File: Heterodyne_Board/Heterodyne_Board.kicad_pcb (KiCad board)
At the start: 2 copper layers, 47 parts, among them J1 AVR-ISP-6, J2 Speaker, J3 SWITCH, U1 ATtiny85-20P, U2 TLV9054xD, U3 AP2112K-3.3, U4 LM386, U5 W25X40CLSN

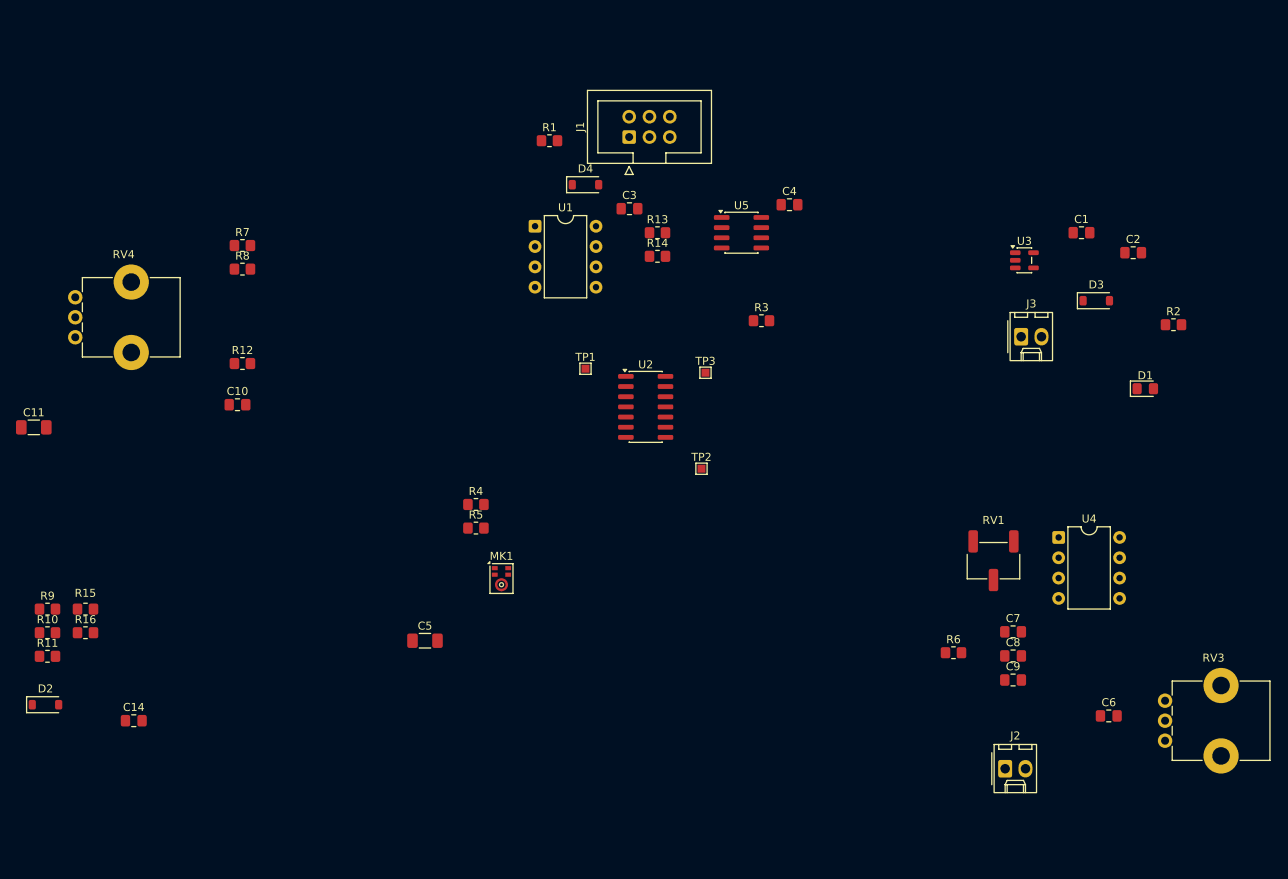
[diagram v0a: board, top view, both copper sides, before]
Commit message: continued PCB design
modules organized except for audio amp, no wiring yet
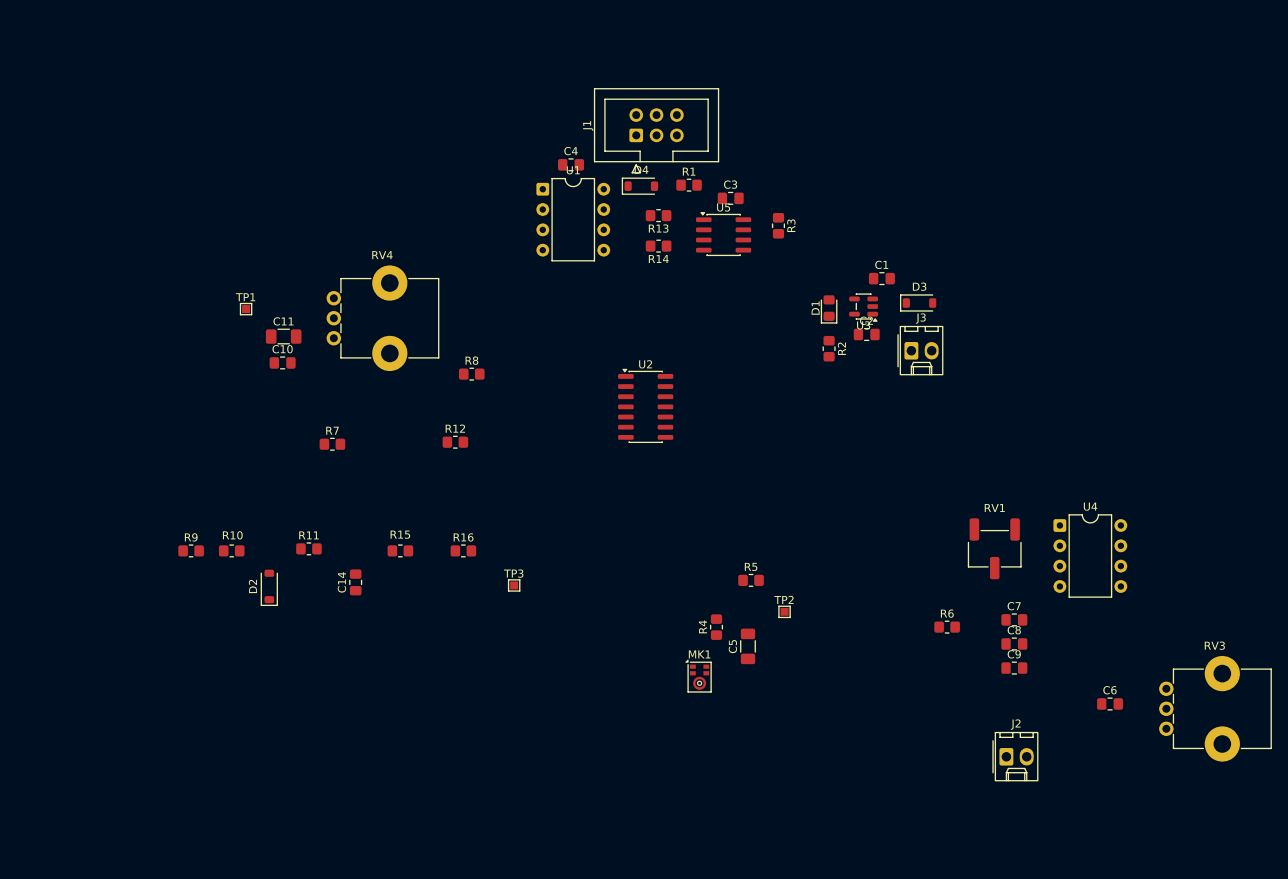
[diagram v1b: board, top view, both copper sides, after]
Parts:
- moved R16 48.3 mm to (121.8, 96.8)
- moved R2 43.2 mm to (167.5, 71.5), turned to -90 degrees
- moved TP1 43.1 mm to (94.6, 66.5)
- moved D1 40.8 mm to (167.5, 66.4), turned to 90 degrees
- moved C5 40.4 mm to (157.4, 108.7), turned to 90 degrees
- moved R15 40.0 mm to (113.9, 96.8)
- moved TP3 35.8 mm to (128.1, 101.1)
- moved R11 35.3 mm to (102.5, 96.5)
- moved R5 35.0 mm to (157.7, 100.5)
- moved C2 34.8 mm to (172.2, 69.7)
- moved R4 33.8 mm to (153.4, 106.3), turned to 90 degrees
- moved C11 33.2 mm to (99.3, 70.0)
- moved C14 32.7 mm to (108.3, 100.7), turned to 90 degrees
- moved RV4 32.3 mm to (105.6, 70.2)
- moved D2 31.6 mm to (97.5, 101.2), turned to 90 degrees
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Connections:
- RV4 pad 2: unconnected-(RV4-Pad2) -> Net-(R8-Pad2)
- RV4 pad 3: Net-(R8-Pad2) -> unconnected-(RV4-Pad3)

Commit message: finished the basic PCB layout
no wiring has been done yet though
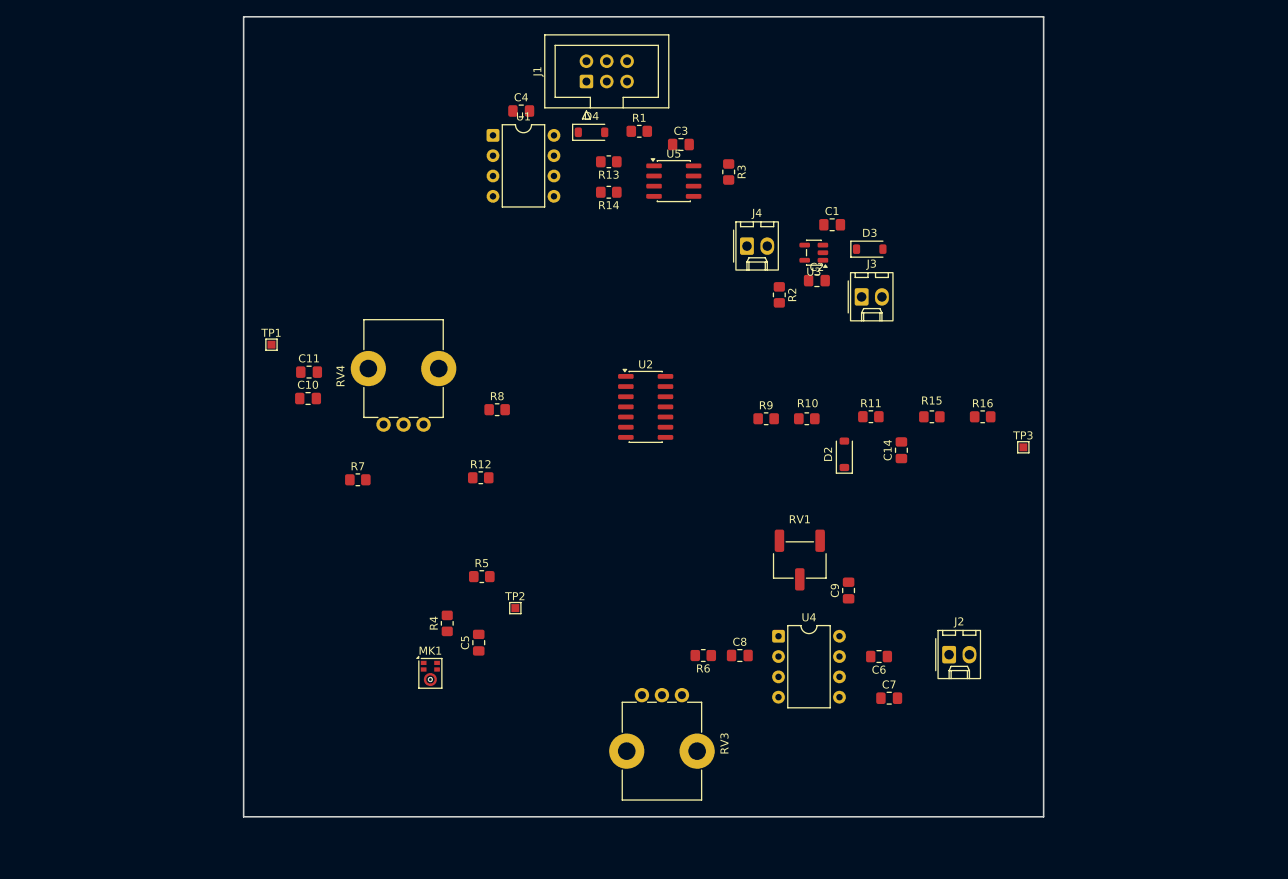
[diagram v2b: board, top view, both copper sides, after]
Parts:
- removed D1: LED, LED_SMD:LED_0805_2012Metric_Pad1.15x1.40mm_HandSolder
- added J4: LED, Connector_Molex:Molex_KK-254_AE-6410-02A_1x02_P2.54mm_Vertical, F.Cu at (157.2, 58.7)
- C11, C5: footprint Capacitor_SMD:C_1206_3216Metric_Pad1.33x1.80mm_HandSolder -> Capacitor_SMD:C_0805_2012Metric_Pad1.18x1.45mm_HandSolder
- moved R10 73.8 mm to (164.7, 80.3)
- moved D2 73.8 mm to (169.4, 84.7)
- moved R9 73.8 mm to (159.6, 80.3)
- moved R11 72.2 mm to (172.7, 80.0)
- moved C14 70.2 mm to (176.5, 84.2)
- moved R15 68.5 mm to (180.3, 80.0)
- moved R16 67.0 mm to (186.7, 80.0)
- moved TP3 65.9 mm to (191.8, 83.8)
- moved RV3 65.7 mm to (144.1, 114.8), turned to -90 degrees
- moved U4 37.8 mm to (161.2, 107.4)
- moved C8 34.3 mm to (156.3, 109.9)
- moved C5 33.7 mm to (123.7, 108.2)
- moved R5 33.7 mm to (124.1, 100.0)
- moved MK1 33.7 mm to (117.7, 112.1)
- moved R4 33.7 mm to (119.8, 105.8)
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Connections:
- R4 pad 2: Net-(U2C--) -> Net-(U2B--)
- R5 pad 1: Net-(U2C--) -> Net-(U2B--)
- U2 pad 10: +3V3 -> unconnected-(U2C-+-Pad10)
- U2 pad 5: unconnected-(U2B-+-Pad5) -> +3V3
- U2 pad 6: unconnected-(U2B---Pad6) -> Net-(U2B--)
- U2 pad 7: unconnected-(U2-Pad7) -> /Mic_out
- U2 pad 8: /Mic_out -> unconnected-(U2-Pad8)
- U2 pad 9: Net-(U2C--) -> unconnected-(U2C---Pad9)
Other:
- board outline added: 100 x 100 mm

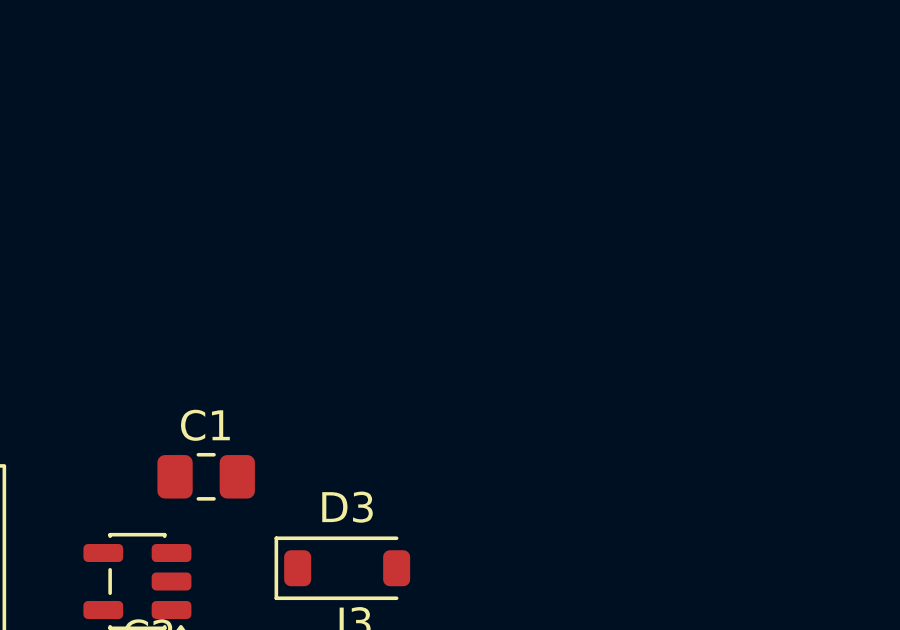
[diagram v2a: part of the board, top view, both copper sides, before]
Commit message: added two new testpoints
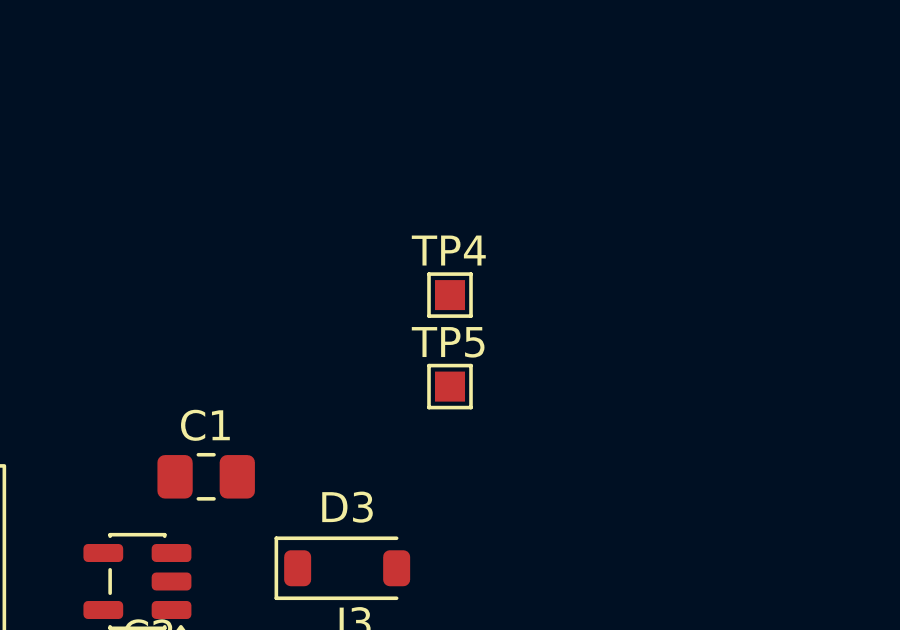
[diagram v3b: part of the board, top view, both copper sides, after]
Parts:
- added TP4: TestPoint, TestPoint:TestPoint_Pad_1.0x1.0mm, F.Cu at (176.0, 50.0)
- added TP5: TestPoint, TestPoint:TestPoint_Pad_1.0x1.0mm, F.Cu at (176.0, 53.0)

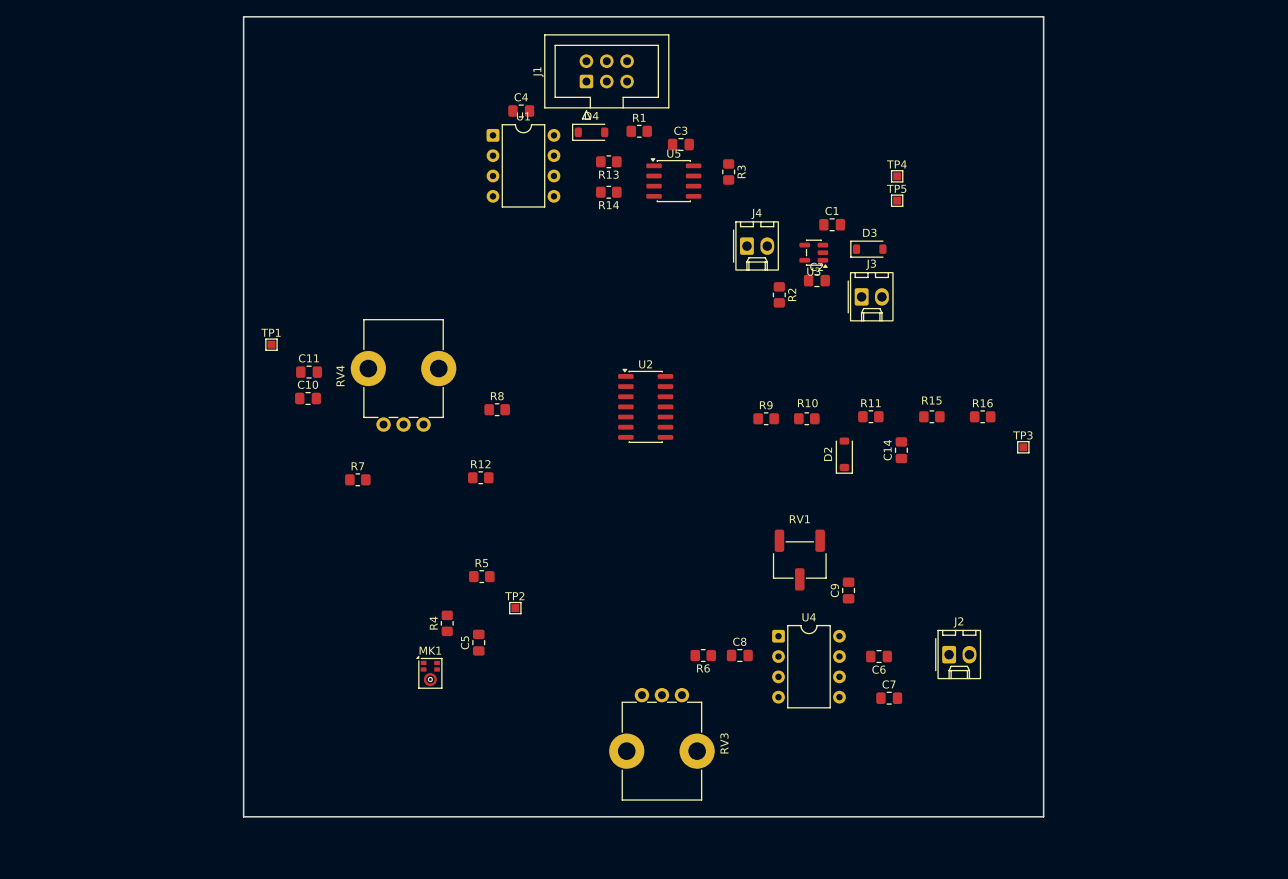
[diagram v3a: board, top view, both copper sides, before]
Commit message: started routing + fixed schematic
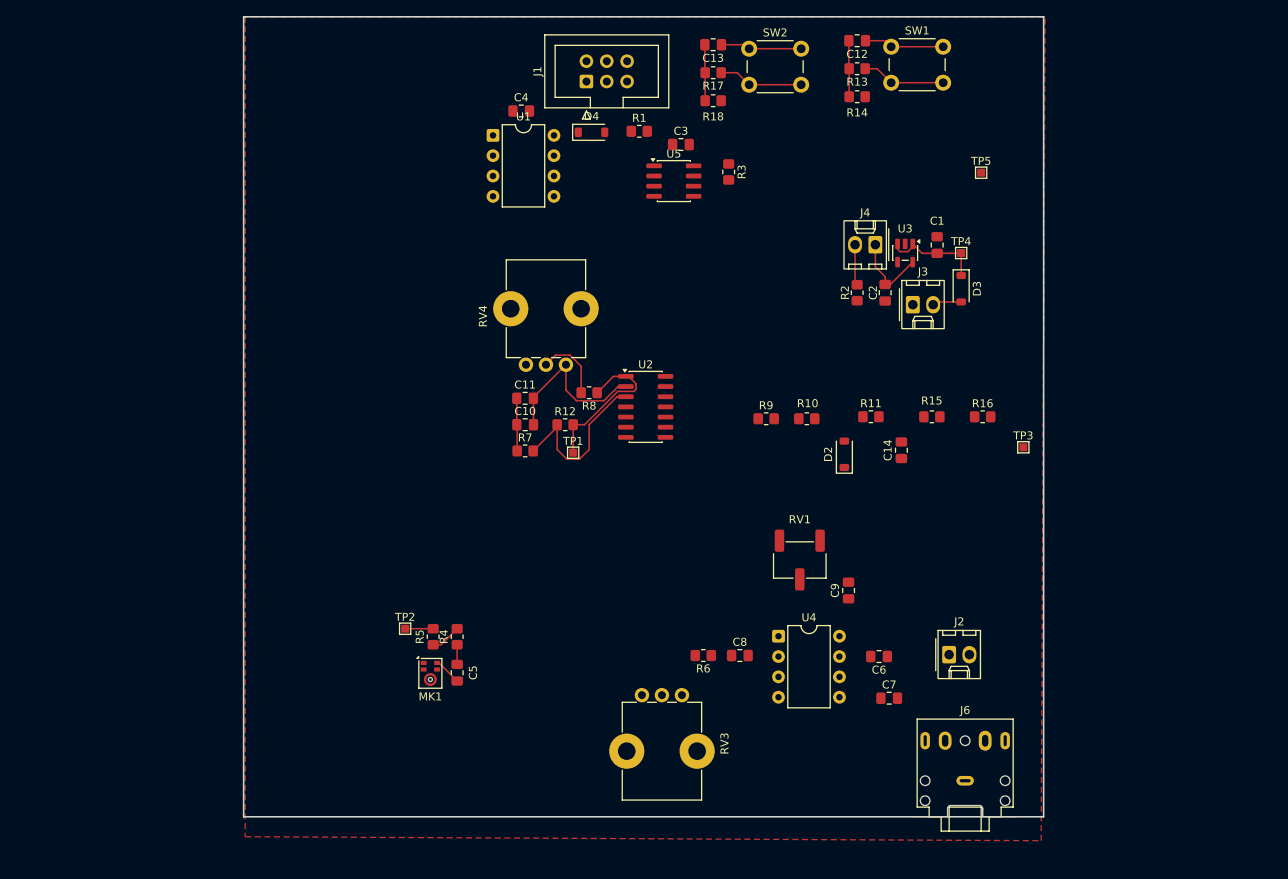
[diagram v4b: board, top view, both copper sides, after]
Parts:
- added C12: 0.1u, Capacitor_SMD:C_0805_2012Metric_Pad1.18x1.45mm_HandSolder, F.Cu at (171.0, 33.0)
- added C13: 0.1u, Capacitor_SMD:C_0805_2012Metric_Pad1.18x1.45mm_HandSolder, F.Cu at (153.0, 33.5)
- added J6: AudioJack2_Ground_Switch, Connector_Audio:Jack_3.5mm_CUI_SJ1-3525N_Horizontal, F.Cu at (184.5, 125.5)
- added R17: 1k, Resistor_SMD:R_0805_2012Metric_Pad1.20x1.40mm_HandSolder, F.Cu at (153.0, 37.0)
- added R18: 10k, Resistor_SMD:R_0805_2012Metric_Pad1.20x1.40mm_HandSolder, F.Cu at (153.0, 40.5)
- added SW1: SW_SPST, Button_Switch_THT:SW_PUSH_6mm_H13mm, F.Cu at (175.2, 33.8)
- added SW2: SW_SPST, Button_Switch_THT:SW_PUSH_6mm_H13mm, F.Cu at (157.5, 34.0)
- R13: value 0 -> 1k
- R14: value 0 -> 10k
- R4: value 3.16k -> 3.3k
- moved TP1 40.1 mm to (135.5, 84.5)
- moved R14 33.3 mm to (171.0, 40.0), turned to 0 degrees
- moved R13 33.2 mm to (171.0, 36.5)
- moved C10 27.3 mm to (129.5, 81.0)
- moved C11 27.2 mm to (129.5, 77.7)
- moved R7 21.2 mm to (129.5, 84.3)
- moved RV4 19.3 mm to (134.6, 73.5)
- moved J4 16.1 mm to (173.3, 58.5), turned to 180 degrees
- moved TP2 14.0 mm to (114.5, 106.5)
- moved C1 13.4 mm to (181.0, 58.5), turned to 90 degrees
- moved TP4 12.5 mm to (184.0, 59.5)
- moved R12 12.5 mm to (134.5, 81.0)
- moved D3 12.5 mm to (184.0, 64.0), turned to -90 degrees
- moved R8 11.7 mm to (137.5, 77.0), turned to 180 degrees
- moved U3 11.4 mm to (177.0, 59.5), turned to -90 degrees
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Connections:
- C7 pad 2: Net-(J2-Pin_1) -> Net-(C7-Pad2)
- R13 pad 1: /CS_in -> Net-(SW1-B)
- R13 pad 2: /CS_out -> /Audio_EN
- R14 pad 1: /WP_in -> /Audio_EN
- R14 pad 2: /WP_out -> +3V3
- U1 pad 2: /CS_out -> /Audio_EN
- U1 pad 3: /WP_out -> /Speaker_in
- U5 pad 1: /CS_in -> GND
- U5 pad 3: /WP_in -> Net-(U5-~{HOLD})
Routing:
- net Net-(U2A-+): track 0.00 -> 21.8 mm
- net Net-(U2A--): track 0.00 -> 21.1 mm
- net GND: track 0.00 -> 20.2 mm
- net /Osci_out: track 0.00 -> 20.0 mm
- net +3V3: track 0.00 -> 16.7 mm
- net Net-(D3-K): track 0.00 -> 12.7 mm
- net Net-(SW2-B): track 0.00 -> 10.6 mm
- net Net-(SW1-B): track 0.00 -> 10.5 mm
- net Net-(R8-Pad2): track 0.00 -> 8.78 mm
- net /RESET: track 0.00 -> 7.02 mm
- net /Audio_EN: track 0.00 -> 7.02 mm
- net Net-(J4-Pin_2): track 0.00 -> 5.11 mm
- net Net-(U2B--): track 0.00 -> 3.83 mm
- net Net-(D3-A): track 0.00 -> 3.64 mm
- net /Mic_out: track 0.00 -> 3.50 mm
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- added copper zone on F.Cu, net GND

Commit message: Pushin P
done with routing!
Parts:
- added J7: Barrel_Jack, Connector_BarrelJack:BarrelJack_Horizontal, F.Cu at (181.4, 84.0)
- moved TP5 64.9 mm to (179.3, 114.0)
- moved D4 53.3 mm to (174.0, 83.5), turned to 90 degrees
- moved C4 50.7 mm to (166.4, 76.0), turned to 180 degrees
- moved R1 47.5 mm to (166.5, 86.0), turned to 180 degrees
- moved C1 45.3 mm to (185.5, 103.6)
- moved TP4 45.3 mm to (188.5, 104.6)
- moved U3 45.3 mm to (181.5, 104.6)
- moved C2 45.3 mm to (179.0, 109.5)
- moved D3 45.3 mm to (188.5, 109.0)
- moved J3 45.3 mm to (182.5, 111.0)
- moved J4 45.3 mm to (177.8, 103.5)
- moved R2 45.3 mm to (175.5, 109.5)
- moved U1 43.5 mm to (155.1, 76.7)
- moved J1 39.2 mm to (162.5, 68.1)
- moved SW2 38.3 mm to (148.8, 71.3), turned to 180 degrees
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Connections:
- D4 pad 1: Net-(D4-K) -> +6V
- D4 pad 2: +5V -> Net-(D4-A)
- J1 pad 2: Net-(D4-K) -> Net-(D4-A)
- R1 pad 1: +5V -> +6V
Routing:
- net +3V3: track 16.7 -> 144.8 mm, vias 0 -> 4
- net +6V: track 0.00 -> 86.0 mm
- net /Speaker_in: track 0.00 -> 76.8 mm, vias 0 -> 4
- net /RESET: track 7.02 -> 52.1 mm
- net /MOSI: track 0.00 -> 30.9 mm, vias 0 -> 2
- net Net-(D4-A): track 0.00 -> 29.2 mm
- net /Audio_EN: track 7.02 -> 34.4 mm, vias 0 -> 2
- net Net-(J2-Pin_1): track 0.00 -> 25.8 mm, vias 0 -> 2
- net /SCK: track 0.00 -> 24.4 mm, vias 0 -> 2
- net /Mic_out: track 3.50 -> 27.9 mm, vias 0 -> 2
- net /MISO: track 0.00 -> 23.6 mm, vias 0 -> 2
- net Net-(C7-Pad2): track 0.00 -> 19.7 mm
- net Net-(U2D--): track 0.00 -> 19.5 mm, vias 0 -> 2
- net GND: track 20.2 -> 0.71 mm, vias 0 -> 1
- net Net-(U5-~{HOLD}): track 0.00 -> 18.2 mm
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- added copper zone on B.Cu, net GND

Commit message: initial pcb design finished
missing a couple things but we ship
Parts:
- removed R1: 10k, Resistor_SMD:R_0805_2012Metric_Pad1.20x1.40mm_HandSolder
- moved TP5 8.76 mm to (184.4, 106.9)
- moved SW1 5.98 mm to (187.8, 71.1), turned to 180 degrees
- moved D3 0.74 mm to (188.5, 109.8)
- moved J3 0.74 mm to (182.5, 111.8)
- moved TP3 0.14 mm to (166.0, 89.4)
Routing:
- net /RESET: track 52.1 -> 27.2 mm, vias 0 -> 2
- net +3V3: track 144.8 -> 139.7 mm
- net Net-(C5-Pad1): track 3.57 -> 8.54 mm, vias 0 -> 2
- net /Speaker_in: track 76.8 -> 81.3 mm
- net /Osci_out: track 28.3 -> 25.0 mm, vias 2 -> 4
- net GND: track 0.71 -> 2.91 mm, vias 1 -> 11
- net Net-(D3-K): track 13.3 -> 15.0 mm, vias 0 -> 2
- net +6V: track 86.0 -> 86.7 mm
- net /SCK: track 24.4 -> 23.9 mm
- net Net-(D4-A): track 29.2 -> 29.7 mm
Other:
- board size 100 x 100 mm -> 57.4 x 69.5 mm
- board text added: "(Osc.)"
- board text added: "(RESET)"
- board text added: "(Vol.)"

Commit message: added switch between mcu and mixer for audio output definition
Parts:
- added U6: TS5A3159DCK, Package_TO_SOT_SMD:SOT-363_SC-70-6, F.Cu at (183.0, 94.5)
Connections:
- R16 pad 2: /Speaker_in -> /Mixer_Out
- TP3 pad 1: /Speaker_in -> /Mixer_Out
- U1 pad 3: /Speaker_in -> /MCU_Out
- U1 pad 5: /MISO -> /MOSI
- U1 pad 6: /MOSI -> /MISO
- U2 pad 14: /Speaker_in -> /Mixer_Out
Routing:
- net /Audio_EN: track 33.9 -> 75.8 mm, vias 2 -> 4
- net /Speaker_in: track 81.3 -> 40.4 mm, vias 4 -> 2
- net /MCU_Out: track 0.00 -> 39.4 mm, vias 0 -> 2
- net /Mixer_Out: track 0.00 -> 20.6 mm, vias 0 -> 2
- net +3V3: track 139.7 -> 149.8 mm
